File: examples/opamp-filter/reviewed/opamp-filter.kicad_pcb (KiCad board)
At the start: 2 copper layers, 58 x 42 mm, 22 parts, among them J1 IN, J2 5V, J3 OUT, U1 MCP6001R, U2 MCP6001R

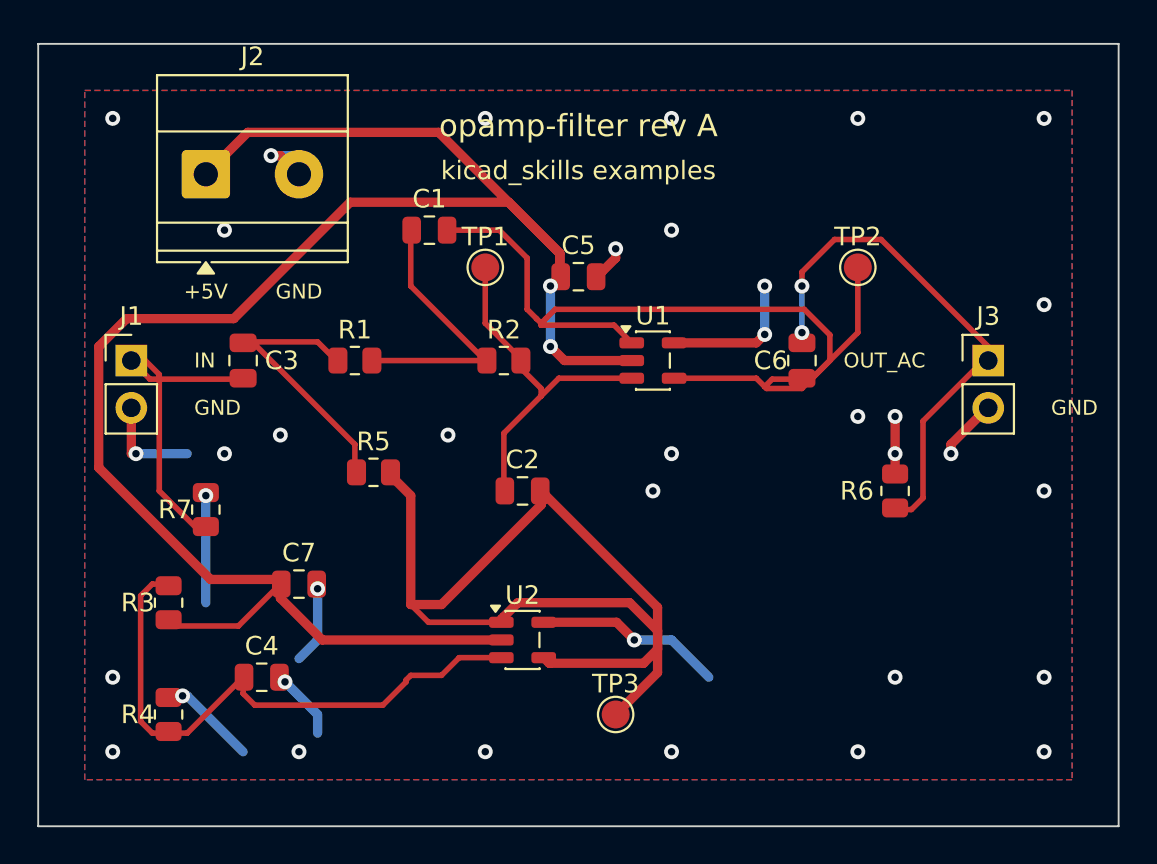
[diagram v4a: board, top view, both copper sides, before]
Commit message: A net may not cross its own copper
The reviewer looked at the plots, saw tracks driven through each other, and
asked whether the other checks were really passing. Both halves of the
answer were worth keeping. Measured directly - every pair of same-layer
segments on every reviewed board - there is not one crossing between
different nets: DRC reports zero errors, zero shorts, zero unconnected, and
it is not being fooled. What the plots show is a net crossing *itself*:
thirteen places on the FPGA board, one each on the op-amp and the buck.
Same potential, so DRC has nothing to say; no length ratio catches it; no
rule of ours looked. The checks were honest. The check list had a hole
exactly the shape of what the eye catches first.

route.self_crossing (new, warning, promoted by ai-generated) measures it:
two branches of one net crossing means the copper carries a redundant loop,
and a person never draws one. KiCad's demo corpus: 6 of 16 boards carry one
to three, at dense escapes.

_unlooped (new pass) is the fix, as a graph question: split every same-net
crossing so the X is a node, and while any cycle remains in the net's
copper, remove the longest junction-to-junction chain of the cycle -
connectivity is kept by definition, a cycle has two ways round, and the
amputated X becomes an ordinary corner. The clearance oracle now also
refuses to let _doglegged or _straighten draw a new X over their own net.

The cutter was wrong twice before it was right, both times the same lesson:
KiCad's connectivity is geometric, a track graph is endpoint topology, and
the difference is exactly a pad. The escape fan draws a micro-hook inside
an off-grid pad - the overlap is the connection - and the graph read it as
a dangling loop and amputated the pad's only feed. Nodes inside an own-net
pad are anchors now, a cycle wholly inside one pad is immune, and segments
passing over a pad are split so the feed is a node the cut must respect.

Self-crossings on the five reviewed boards: 0/0/0/0/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
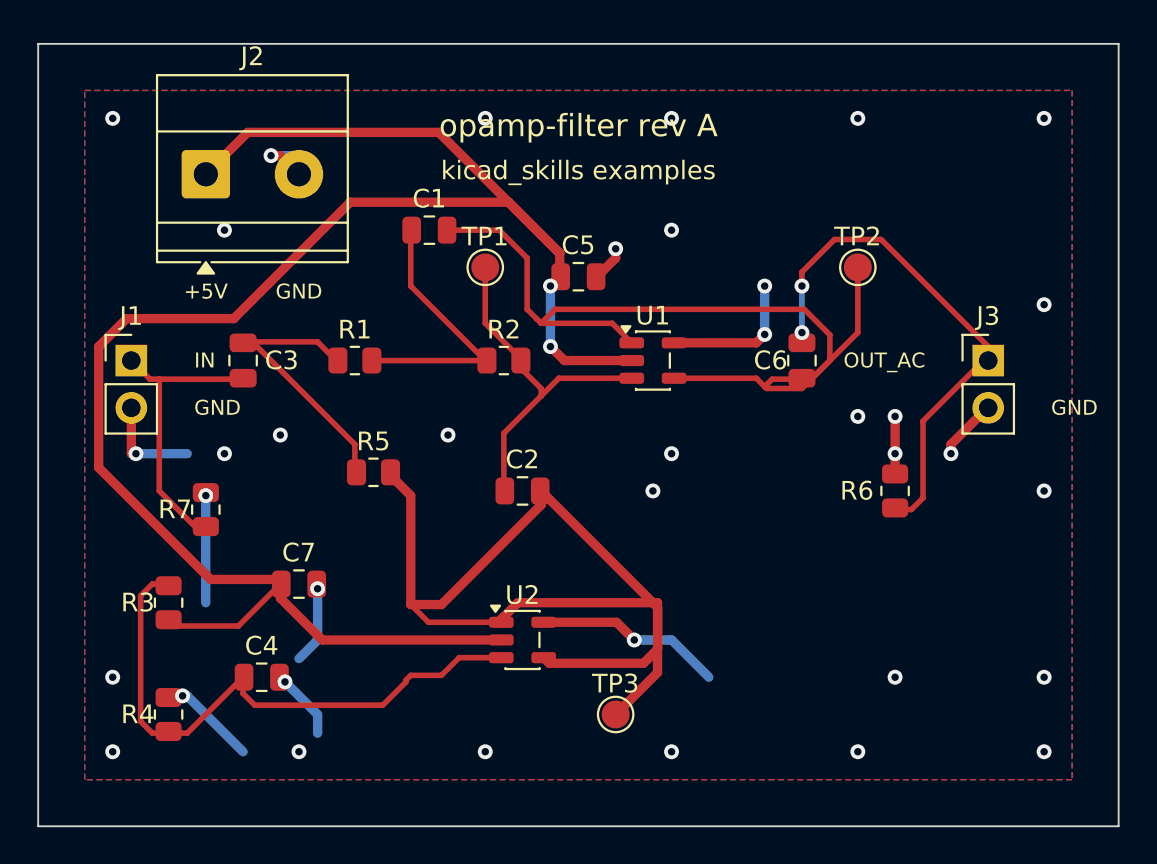
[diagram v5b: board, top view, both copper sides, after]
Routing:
- net /IN: track 17.9 -> 15.8 mm
- net +5V: track 102.6 -> 101.6 mm
- net /VREF: track 55.4 -> 56.3 mm
